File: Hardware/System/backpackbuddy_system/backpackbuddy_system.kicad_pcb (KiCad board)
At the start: 2 copper layers, 65 x 56 mm, 76 parts, among them J1 PIR, J10 USB_B_Micro, J11 Battery, J2 Ultrasonic 2, J3 Ultrasonic 1, J4 Left Vibration 1, J5 Left Vibration 2, J6 RPi_GPIO, J7 ESP8266, J8 Right Vibration 1, J9 Right Vibration 2, Q1 Q_NMOS_GSD, Q2 Q_NMOS_GSD, Q3 SIHF9Z24STRR-GE3, SW1 ESP8266 RESET, SW2 MCU RESET, U1 ATmega32U4-A, U2 SI-8050Y, U3 LM3940, Y1 16MHz

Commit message: decoupling caps
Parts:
- added R14: 10k, Resistor_SMD:R_0603_1608Metric_Pad0.98x0.95mm_HandSolder, F.Cu at (125.7, 79.2)
- C1, C2, L1, U1, Y1: moved to B.Cu
- moved J1 130.4 mm to (159.2, 113.8), turned to 90 degrees
- moved U2 107.2 mm to (157.5, 72.4)
- moved C13 101.3 mm to (158.8, 88.9)
- moved D4 100.9 mm to (158.8, 81.8)
- moved J11 99.9 mm to (173.6, 69.9)
- moved D9 95.5 mm to (144.7, 103.5)
- moved D12 95.4 mm to (140.2, 103.4)
- moved D11 94.5 mm to (134.9, 103.4)
- moved D10 93.5 mm to (129.5, 102.9)
- moved J2 93.0 mm to (139.7, 113.8), turned to 90 degrees
- moved C6 88.2 mm to (134.9, 74.9)
- moved J5 82.9 mm to (118.1, 100.3)
- moved J10 82.7 mm to (171.0, 85.2), turned to 90 degrees
- moved J4 73.6 mm to (113.3, 100.3)
- moved J3 73.0 mm to (120.7, 113.8), turned to 90 degrees
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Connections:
- J6 pad 1: /Raspberry Pi/3v3 -> +3V3
- J6 pad 14: /Raspberry Pi/gnd -> GND
- J6 pad 17: /Raspberry Pi/3v3 -> +3V3
- J6 pad 2: /Raspberry Pi/5v -> +5V
- J6 pad 20: /Raspberry Pi/gnd -> GND
- J6 pad 25: /Raspberry Pi/gnd -> GND
- J6 pad 3: unconnected-(J6-Pad3) -> /Raspberry Pi/GPIO2_SDA
- J6 pad 30: /Raspberry Pi/gnd -> GND
- J6 pad 34: /Raspberry Pi/gnd -> GND
- J6 pad 39: /Raspberry Pi/gnd -> GND
- J6 pad 4: /Raspberry Pi/5v -> +5V
- J6 pad 5: unconnected-(J6-Pad5) -> /Raspberry Pi/GPIO3_SCL
- J6 pad 6: /Raspberry Pi/gnd -> GND
- J6 pad 7: unconnected-(J6-Pad7) -> /Raspberry Pi/GPIO4_GPCLK0
- J6 pad 9: /Raspberry Pi/gnd -> GND
- SW1 pad 2: GND -> +3V3

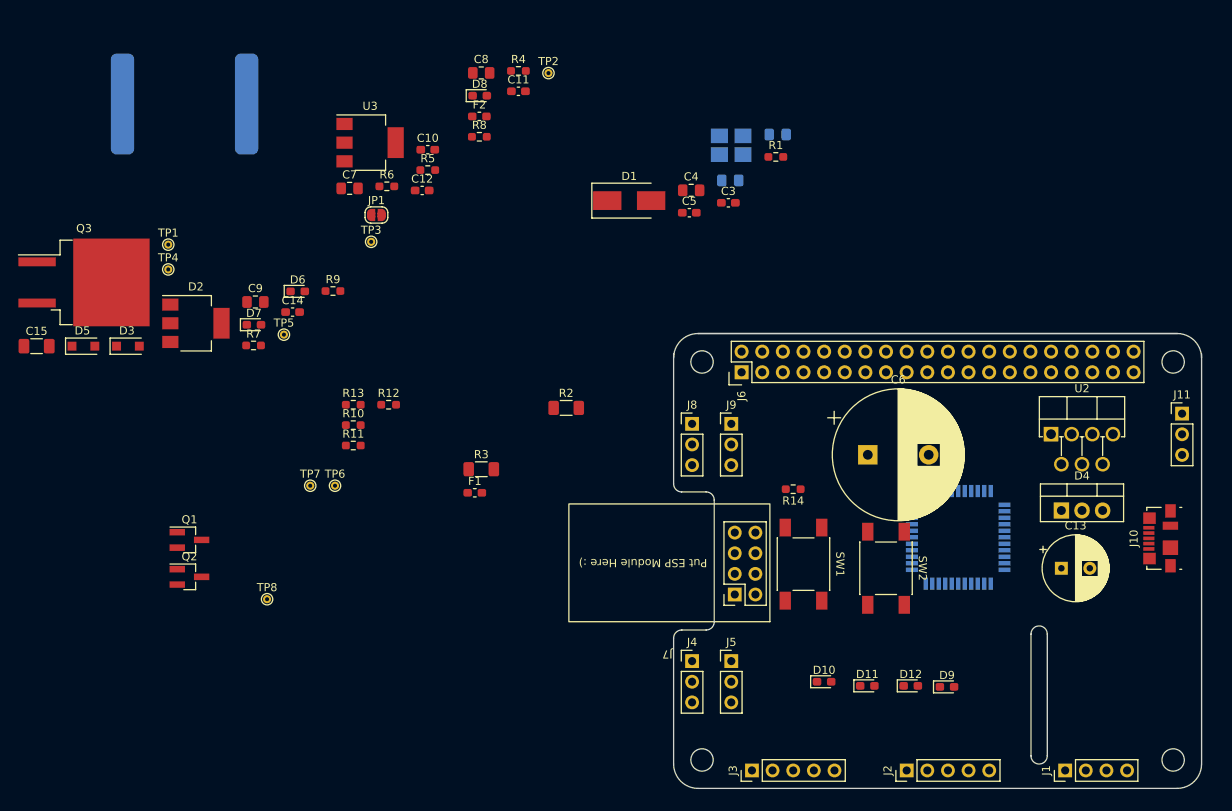
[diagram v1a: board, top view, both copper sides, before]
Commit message: board outline redo
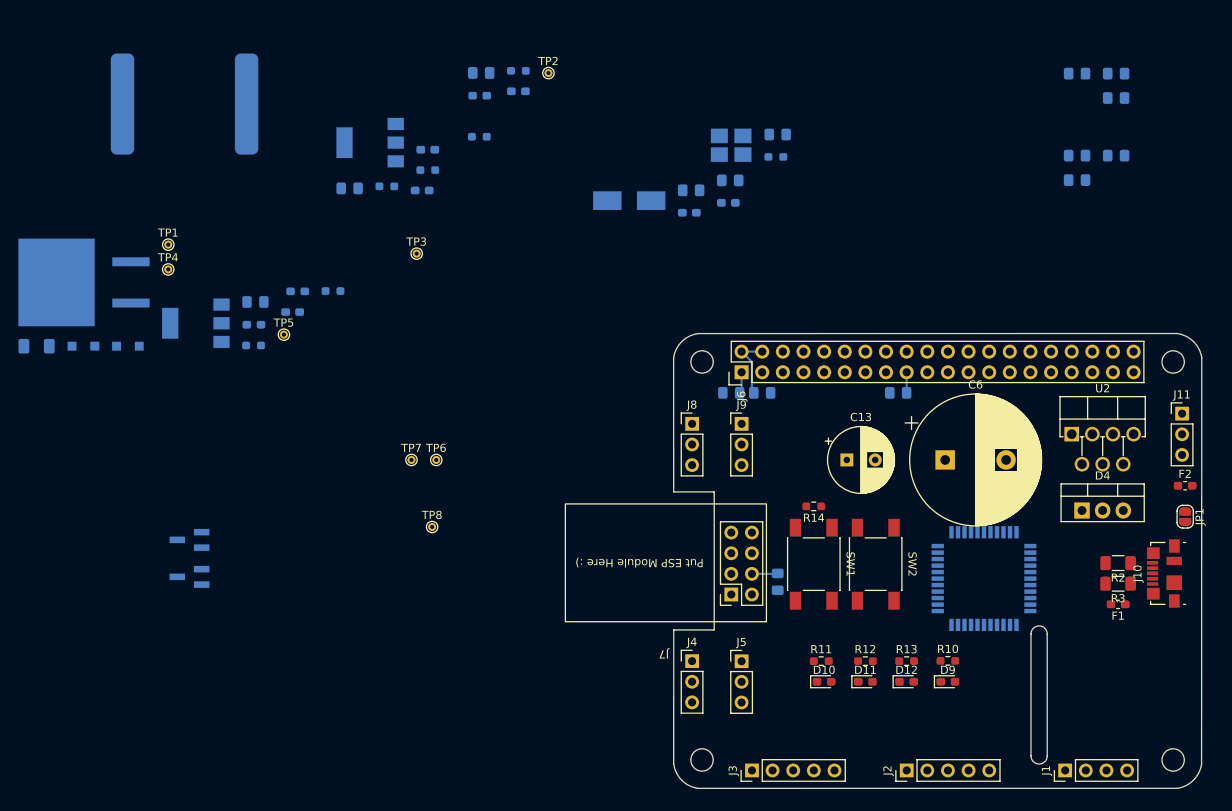
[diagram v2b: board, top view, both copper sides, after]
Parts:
- added C16: 10uF, Capacitor_SMD:C_0805_2012Metric_Pad1.18x1.45mm_HandSolder, B.Cu at (160.7, 38.1)
- added C17: 10uF, Capacitor_SMD:C_0805_2012Metric_Pad1.18x1.45mm_HandSolder, B.Cu at (160.7, 41.1)
- added C18: 10uF, Capacitor_SMD:C_0805_2012Metric_Pad1.18x1.45mm_HandSolder, B.Cu at (165.5, 38.1)
- added C19: 10uF, Capacitor_SMD:C_0805_2012Metric_Pad1.18x1.45mm_HandSolder, B.Cu at (123.8, 90.6)
- added C20: 10uF, Capacitor_SMD:C_0805_2012Metric_Pad1.18x1.45mm_HandSolder, B.Cu at (165.5, 28.0)
- added C21: 10uF, Capacitor_SMD:C_0805_2012Metric_Pad1.18x1.45mm_HandSolder, B.Cu at (160.7, 28.0)
- added C22: 10uF, Capacitor_SMD:C_0805_2012Metric_Pad1.18x1.45mm_HandSolder, B.Cu at (165.5, 31.0)
- added C23: 10uF, Capacitor_SMD:C_0805_2012Metric_Pad1.18x1.45mm_HandSolder, B.Cu at (121.9, 67.3)
- added C24: 10uF, Capacitor_SMD:C_0805_2012Metric_Pad1.18x1.45mm_HandSolder, B.Cu at (138.7, 67.3)
- added C25: 10uF, Capacitor_SMD:C_0805_2012Metric_Pad1.18x1.45mm_HandSolder, B.Cu at (118.1, 67.3)
- C10, C11, C12, C14, C15, C3, C4, C5, C7, C8, C9, D1, D2, D3, D5, D6, D7, D8, Q1, Q2, Q3, R1, R4, R5, R6, R7, R8, R9, U3: moved to B.Cu
- moved JP1 106.3 mm to (174.0, 82.5), turned to -90 degrees
- moved F2 98.1 mm to (174.0, 78.7)
- moved F1 80.4 mm to (165.7, 93.3), turned to 180 degrees
- moved R3 79.7 mm to (165.7, 90.8), turned to 180 degrees
- moved R10 78.7 mm to (144.8, 100.3)
- moved R13 75.1 mm to (139.7, 100.3)
- moved R2 70.6 mm to (165.7, 88.3), turned to 180 degrees
- moved R12 66.6 mm to (134.6, 100.3)
- moved R11 63.4 mm to (129.2, 100.3)
- moved C13 29.6 mm to (132.3, 75.6)
- moved TP8 22.2 mm to (81.3, 83.8)
- moved TP6 12.9 mm to (81.8, 75.6)
- moved TP7 12.9 mm to (78.7, 75.6)
- moved C6 9.55 mm to (144.4, 75.6)
- moved U1 5.99 mm to (149.2, 90.2)
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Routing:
- net +5V: track 0.00 -> 8.24 mm
- net +3V3: track 0.00 -> 7.94 mm
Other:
- outline, holes or cut-outs redrawn

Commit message: components placed time to wire
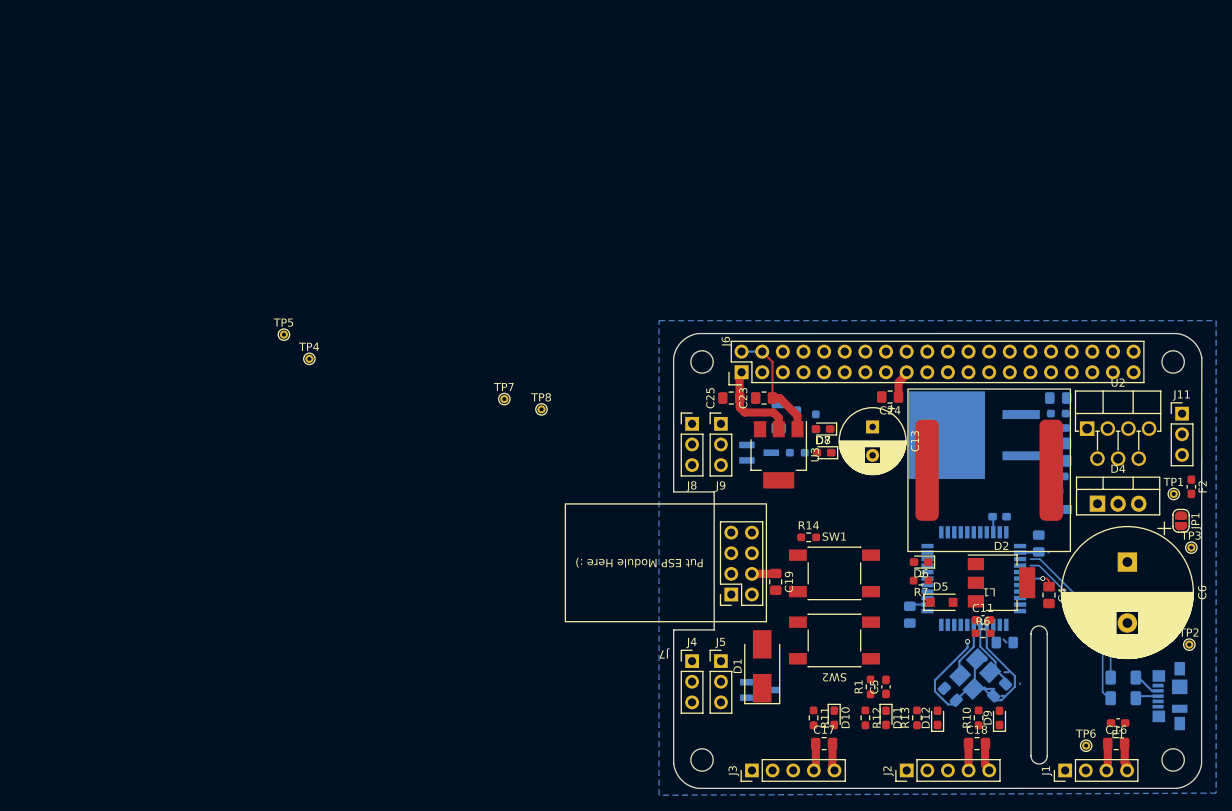
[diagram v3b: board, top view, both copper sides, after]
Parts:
- C11, C16, C17, C18, C19, C23, C24, C25, C4, C5, D1, D2, D5, D6, D7, D8, L1, R1, R6, R7, U3: moved to F.Cu
- J10, R2, R3: moved to B.Cu
- moved TP1 127.5 mm to (172.6, 79.8)
- moved D3 116.0 mm to (158.1, 81.7)
- moved Q3 111.2 mm to (148.0, 72.5)
- moved D5 110.3 mm to (144.0, 93.1), turned to 0 degrees
- moved L1 108.8 mm to (149.9, 76.8)
- moved TP2 105.7 mm to (174.5, 98.3)
- moved D2 104.2 mm to (151.4, 90.7), turned to 0 degrees
- moved TP3 102.0 mm to (174.8, 86.4)
- moved C9 100.3 mm to (158.3, 73.5)
- moved C7 93.5 mm to (158.4, 75.7)
- moved C15 91.8 mm to (124.0, 70.1), turned to 90 degrees
- moved R6 91.7 mm to (149.1, 96.9), turned to 0 degrees
- moved TP6 87.4 mm to (161.8, 110.7)
- moved R7 87.1 mm to (141.5, 90.4)
- moved C11 86.6 mm to (149.1, 95.2), turned to 0 degrees
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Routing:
- net GND: track 0.00 -> 44.2 mm, vias 0 -> 1
- net +5V: track 8.24 -> 31.7 mm
- net /microcontroller/D+: track 0.00 -> 21.1 mm
- net /microcontroller/D-: track 0.00 -> 19.1 mm
- net +3V3: track 7.94 -> 17.6 mm
- net Net-(C2-Pad2): track 0.00 -> 8.91 mm
- net Net-(C1-Pad2): track 0.00 -> 7.04 mm
- net Net-(J10-Pad2): track 0.00 -> 3.42 mm
- net Net-(C4-Pad1): track 0.00 -> 3.15 mm, vias 0 -> 1
- net Net-(J10-Pad3): track 0.00 -> 2.85 mm
- net Net-(C3-Pad1): track 0.00 -> 1.96 mm
- added copper zone on B.Cu, net GND

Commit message: almost done
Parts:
- removed C25: 10uF, Capacitor_SMD:C_0805_2012Metric_Pad1.18x1.45mm_HandSolder
- R10, R11, R12, R13: moved to B.Cu
- moved C24 19.6 mm to (118.1, 67.9)
- moved C5 6.75 mm to (130.6, 102.1), turned to 180 degrees
- moved F1 5.76 mm to (167.1, 102.4)
- moved R4 3.81 mm to (158.4, 73.7)
- moved C9 3.43 mm to (158.4, 70.1)
- moved D8 3.43 mm to (129.5, 78.1), turned to 0 degrees
- moved D7 2.92 mm to (129.4, 68.8), turned to 0 degrees
- moved R11 2.47 mm to (130.7, 107.7)
- moved D9 2.19 mm to (149.0, 107.7), turned to -90 degrees
- moved C12 2.16 mm to (158.4, 75.4)
- moved TP1 2.16 mm to (174.8, 79.8)
- moved F2 2.03 mm to (172.7, 78.9)
- moved C3 1.92 mm to (149.2, 82.5), turned to 180 degrees
- moved R1 1.81 mm to (134.1, 102.1), turned to 0 degrees
- moved C7 1.78 mm to (158.4, 77.5)
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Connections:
- J1 pad 2: /microcontroller/PB2 -> /microcontroller/PB7
- J2 pad 2: /microcontroller/PD5 -> /PD5
- R10 pad 1: /microcontroller/PB3 -> /microcontroller/PD0
- R13 pad 1: /microcontroller/PB6 -> /microcontroller/PD3/TX
- R14 pad 1: /ESP RESET -> +3V3
- R14 pad 2: GND -> /ESP RESET
- SW1 pad 2: +3V3 -> GND
- TP6 pad 1: /microcontroller/PB2 -> /microcontroller/PB7
- U1 pad 12: unconnected-(U1-Pad12) -> /microcontroller/PB7
- U1 pad 22: /microcontroller/PD5 -> unconnected-(U1-Pad22)
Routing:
- net GND: track 44.2 -> 175.6 mm, vias 1 -> 15
- net /Power/18V PROTECTED: track 0.00 -> 79.1 mm, vias 0 -> 1
- net Net-(D2-Pad2): track 0.00 -> 46.4 mm, vias 0 -> 1
- net +3V3: track 17.6 -> 55.5 mm, vias 0 -> 2
- net +5V: track 31.7 -> 66.8 mm, vias 0 -> 7
- net Net-(C12-Pad2): track 0.00 -> 23.4 mm, vias 0 -> 1
- net /ESP RESET: track 0.00 -> 19.5 mm, vias 0 -> 1
- net Net-(D3-Pad2): track 0.00 -> 17.0 mm
- net /microcontroller/~{RESET}: track 0.00 -> 17.0 mm
- net Net-(C8-Pad1): track 0.00 -> 11.7 mm
- net Net-(C10-Pad1): track 0.00 -> 10.9 mm
- net Net-(J4-Pad2): track 0.00 -> 6.89 mm
- net Net-(C11-Pad1): track 0.00 -> 6.81 mm
- net Net-(J8-Pad2): track 0.00 -> 6.78 mm
- net Net-(R9-Pad2): track 0.00 -> 5.30 mm, vias 0 -> 1
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- added copper zone on F.Cu, net +3V3
- added copper zone on F.Cu, net +5V
- added copper zone on F.Cu, net Net-(F2-Pad1)

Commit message: first draft done :))) still errors but thats because i was too lazy to do no connects as of rn
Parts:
- removed D9: Blue, LED_SMD:LED_0603_1608Metric_Pad1.05x0.95mm_HandSolder
- added JP2: PP Short, Jumper:SolderJumper-2_P1.3mm_Open_RoundedPad1.0x1.5mm, B.Cu at (125.6, 84.5)
- added R15: 1k, Resistor_SMD:R_0603_1608Metric_Pad0.98x0.95mm_HandSolder, B.Cu at (122.2, 81.8)
- added R16: 1k, Resistor_SMD:R_0603_1608Metric_Pad0.98x0.95mm_HandSolder, B.Cu at (118.5, 81.8)
- moved TP4 70.5 mm to (134.6, 80.0)
- moved TP5 51.2 mm to (113.6, 68.0)
- moved TP7 41.7 mm to (131.9, 67.7)
- moved TP8 39.4 mm to (134.1, 67.6)
- moved R10 33.5 mm to (123.2, 84.5), turned to 90 degrees
- moved D10 27.1 mm to (132.8, 80.6), turned to 90 degrees
- moved D11 27.1 mm to (138.0, 80.6), turned to 90 degrees
- moved R11 27.1 mm to (131.2, 80.6), turned to 90 degrees
- moved R12 27.1 mm to (136.4, 80.6), turned to 90 degrees
- moved C19 9.88 mm to (119.6, 81.5), turned to 180 degrees
- moved D12 3.53 mm to (138.9, 109.1)
- moved R13 1.42 mm to (140.7, 109.1)
- moved D7 0.63 mm to (129.0, 69.3)
- moved C14 0.21 mm to (126.0, 70.7)
- moved C21 0.10 mm to (156.7, 86.5)
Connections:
- J2 pad 2: /PD5 -> /microcontroller/PD1
- J2 pad 3: /microcontroller/PD4 -> /microcontroller/PD0
- J3 pad 2: /microcontroller/PD1 -> /microcontroller/PD7
- J3 pad 3: /microcontroller/PD0 -> /microcontroller/PD6
- J7 pad 3: /microcontroller/PB0 -> unconnected-(J7-Pad3)
- J7 pad 5: /microcontroller/PB1 -> /microcontroller/PB5
- J7 pad 7: /microcontroller/PD2/RX -> /ESP_RX
- Q1 pad 1: /microcontroller/PF5 -> /microcontroller/PB4
- Q2 pad 1: /microcontroller/PF6 -> /microcontroller/PB6
- R10 pad 1: /microcontroller/PD0 -> /PD2/RX
- R10 pad 2: Net-(D9-Pad2) -> /ESP_RX
- R11 pad 1: /microcontroller/PB4 -> /microcontroller/PF7
- R12 pad 1: /microcontroller/PB5 -> /microcontroller/PF5
- R13 pad 1: /microcontroller/PD3/TX -> /microcontroller/PD4
- TP7 pad 1: /microcontroller/PD6 -> /Raspberry Pi/GPIO17
- TP8 pad 1: /microcontroller/PD7 -> /Raspberry Pi/GPIO27
- U1 pad 20: /microcontroller/PD2/RX -> /PD2/RX
- U1 pad 31: unconnected-(U1-Pad31) -> /Raspberry Pi/GPIO17
- U1 pad 32: unconnected-(U1-Pad32) -> /Raspberry Pi/GPIO27
- U1 pad 36: unconnected-(U1-Pad36) -> /microcontroller/PF7
- U1 pad 37: /microcontroller/PF6 -> /Raspberry Pi/GPIO22
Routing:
- net GND: track 175.6 -> 232.9 mm, vias 15 -> 21
- net /Raspberry Pi/GPIO22: track 0.00 -> 39.4 mm
- net /Raspberry Pi/GPIO17: track 0.00 -> 36.4 mm
- net /Raspberry Pi/GPIO27: track 0.00 -> 36.0 mm
- net /PD2/RX: track 0.00 -> 35.2 mm, vias 0 -> 4
- net /microcontroller/PD7: track 0.00 -> 33.4 mm
- net /microcontroller/PB4: track 0.00 -> 32.4 mm
- net /microcontroller/PD3/TX: track 0.00 -> 31.2 mm, vias 0 -> 2
- net /microcontroller/PB7: track 3.06 -> 34.0 mm
- net /microcontroller/PB6: track 0.00 -> 30.8 mm
- net /microcontroller/PD6: track 0.00 -> 30.6 mm
- net /microcontroller/PD4: track 0.00 -> 30.1 mm
- net /microcontroller/PB5: track 0.00 -> 25.1 mm
- net /microcontroller/PF5: track 0.00 -> 23.0 mm
- net /microcontroller/~{RESET}: track 17.0 -> 40.0 mm, vias 0 -> 3
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
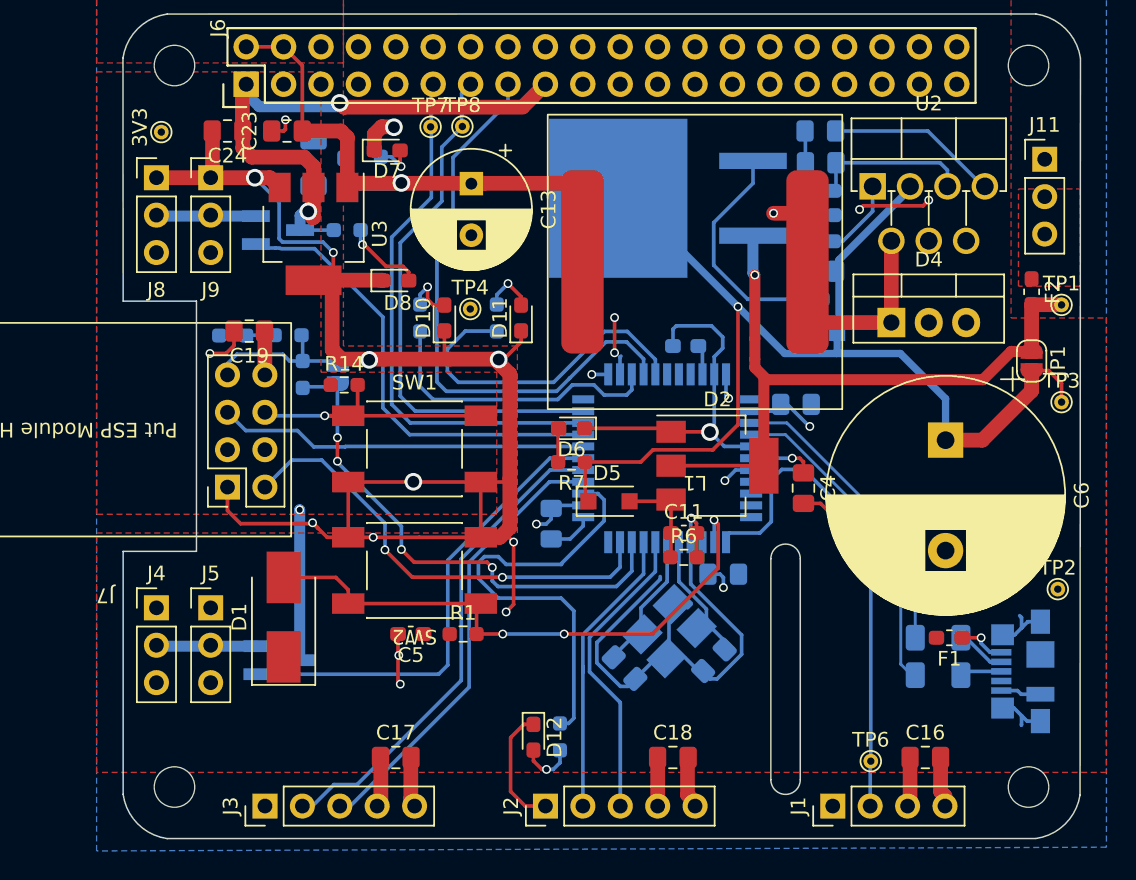
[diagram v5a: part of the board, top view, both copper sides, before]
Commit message: silkscreen done
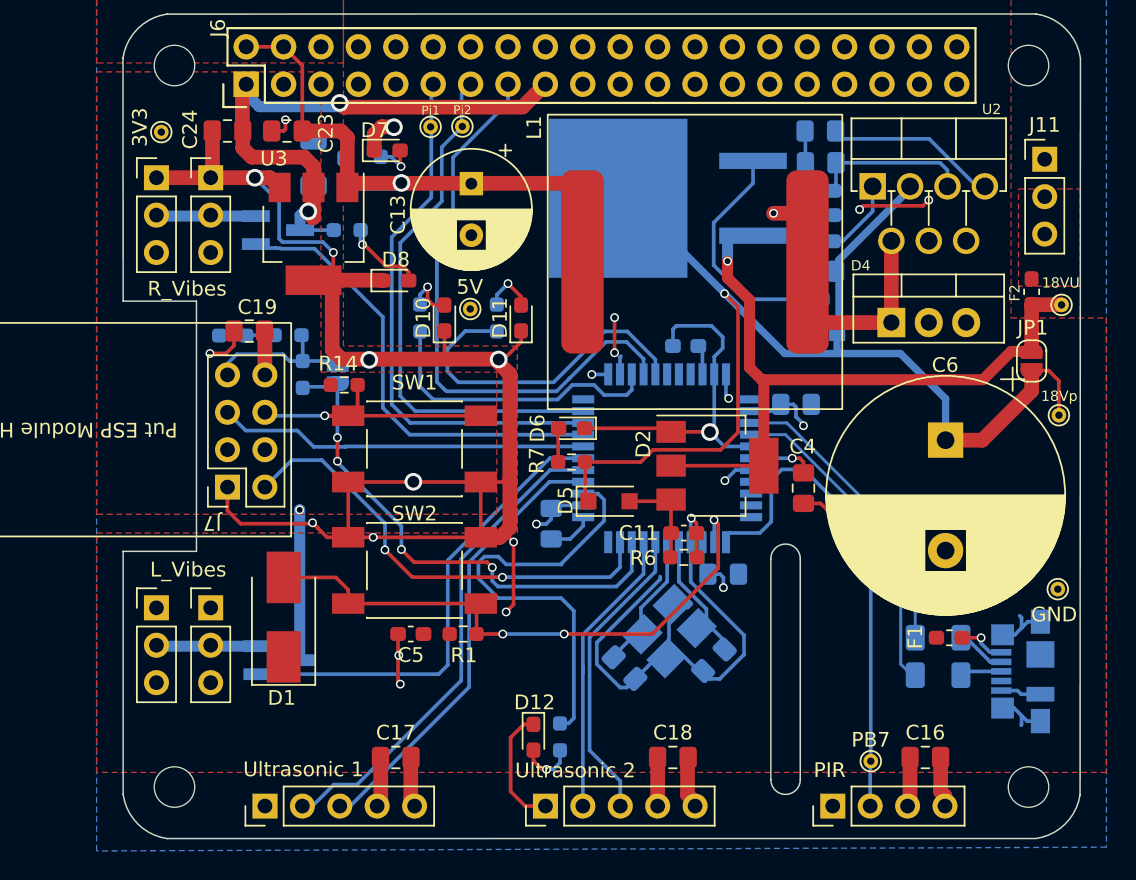
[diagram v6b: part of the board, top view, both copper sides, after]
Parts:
- J4: value Left Vibration 1 -> L_Vibes
- J8: value Right Vibration 1 -> R_Vibes
- TP1: value 9V Unprotected -> 18VU
- TP3: value Protected 9V -> 18Vp
- TP7: value Pi 1 -> Pi1
- TP8: value Pi 2 -> Pi2
- moved TP3 0.91 mm to (174.6, 87.2)
- gave numbers to parts that had none: 4
- renumbered TP6 to PB7
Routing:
- net Net-(D2-Pad2): track 46.4 -> 48.9 mm
- net /Power/18V PROTECTED: track 79.5 -> 81.9 mm

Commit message: minor thingies
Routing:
- net /microcontroller/D-: track 20.4 -> 21.3 mm
- net GND: track 233.2 -> 232.4 mm

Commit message: pushing
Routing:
- net GND: track 232.4 -> 230.3 mm, vias 21 -> 23
- net Net-(D2-Pad2): track 48.9 -> 50.3 mm
